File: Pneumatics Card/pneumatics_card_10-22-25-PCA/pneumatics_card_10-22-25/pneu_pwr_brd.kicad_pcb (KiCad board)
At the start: 2 copper layers, 47.6 x 53.5 mm, 38 parts, among them J1 2X1, J2 2X1, J3 2X1, J4 2X1, J5 2X1, J6 2X1, Q1 BSS138, Q2 BSS138, Q3 FQP30N06L, Q4 FQP30N06L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

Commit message: old pneumatics fixing PCB
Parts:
- removed J1: 2X1, Connector_JST:JST_PH_B2B-PH-K_1x02_P2.00mm_Vertical
- removed Q1, Q2: BSS138, Package_TO_SOT_SMD:SOT-23_Handsoldering
- removed R1, R2: 4.7k, Resistor_SMD:R_0805_2012Metric_Pad1.20x1.40mm_HandSolder
- removed REF** (x3): MountingHole_2.2mm_M2, MountingHole:MountingHole_2.2mm_M2
- added C10: 1uF, Capacitor_SMD:C_0402_1005Metric, F.Cu at (162.1, 31.2)
- added C11: 0.1uF, Capacitor_SMD:C_0402_1005Metric, F.Cu at (162.1, 33.2)
- added C12: 1uF, Capacitor_SMD:C_0402_1005Metric, F.Cu at (162.1, 35.2)
- added C13: 1uF, Capacitor_SMD:C_0402_1005Metric, F.Cu at (162.1, 37.1)
- added C14: 0.1uF, Capacitor_SMD:C_0402_1005Metric, F.Cu at (162.1, 39.1)
- added C16: 0.1u, Capacitor_SMD:C_0603_1608Metric, F.Cu at (153.5, 28.1)
- added C5: 1u, Capacitor_THT:CP_Radial_D5.0mm_P2.00mm, F.Cu at (173.8, 37.8)
- added C6: 0.1u, Capacitor_SMD:C_0603_1608Metric, F.Cu at (153.5, 25.6)
- added C7: 0.1uF, Capacitor_SMD:C_0402_1005Metric, F.Cu at (162.1, 25.3)
- added C8: 1uF, Capacitor_SMD:C_0402_1005Metric, F.Cu at (162.1, 27.3)
- added C9: 0.1uF, Capacitor_SMD:C_0402_1005Metric, F.Cu at (162.1, 29.2)
- added D5: 1N47xxA, Diode_THT:D_DO-41_SOD81_P10.16mm_Horizontal, F.Cu at (165.4, 26.4)
- added J7: 2X1, Connector_JST:JST_PH_B2B-PH-K_1x02_P2.00mm_Vertical, F.Cu at (166.5, 37.2)
- added Q7: IRF4905SPbF, Package_TO_SOT_THT:TO-220-3_Vertical, F.Cu at (166.8, 32.5)
- added R12: 100k, Resistor_SMD:R_0805_2012Metric_Pad1.20x1.40mm_HandSolder, F.Cu at (173.9, 42.5)
- added R13: 100k, Resistor_SMD:R_0805_2012Metric_Pad1.20x1.40mm_HandSolder, F.Cu at (173.9, 45.5)
- added R14: 10k, Resistor_SMD:R_0603_1608Metric, F.Cu at (153.5, 30.6)
- added R155: 10k, Resistor_SMD:R_0603_1608Metric, F.Cu at (153.5, 43.1)
- added R16: 10k, Resistor_SMD:R_0603_1608Metric, F.Cu at (153.5, 33.1)
- added R17: 10k, Resistor_SMD:R_0603_1608Metric, F.Cu at (153.5, 35.6)
- added R18: 10k, Resistor_SMD:R_0603_1608Metric, F.Cu at (153.5, 38.1)
- added R20: 10k, Resistor_SMD:R_0603_1608Metric, F.Cu at (153.5, 40.6)
- added U4: MCP1416, Package_TO_SOT_SMD:SOT-23-5, F.Cu at (158.1, 26.7)
- added U5: TCA4307, TCA4307:SOP65P490X110-8N, F.Cu at (167.8, 43.4)
- added U6: MCP1416, Package_TO_SOT_SMD:SOT-23-5, F.Cu at (158.1, 31.4)
- added U7: MCP1416, Package_TO_SOT_SMD:SOT-23-5, F.Cu at (158.1, 36.0)
- added U8: MCP1416, Package_TO_SOT_SMD:SOT-23-5, F.Cu at (158.1, 40.6)
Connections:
- F1 pad 2: SLN1+ -> Net-(D5-A)
- R10 pad 1: S4CTRL -> Net-(U8-OUT)
- R4 pad 1: S1CTRL -> Net-(U4-OUT)
- R6 pad 1: S2CTRL -> Net-(U6-OUT)
- R8 pad 1: S3CTRL -> Net-(U7-OUT)
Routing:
- net (no net): track 0.00 -> 48.5 mm
- net Net-(J1-Pin_2): track 29.8 -> 0.00 mm
- net Net-(J1-Pin_1): track 18.7 -> 0.00 mm

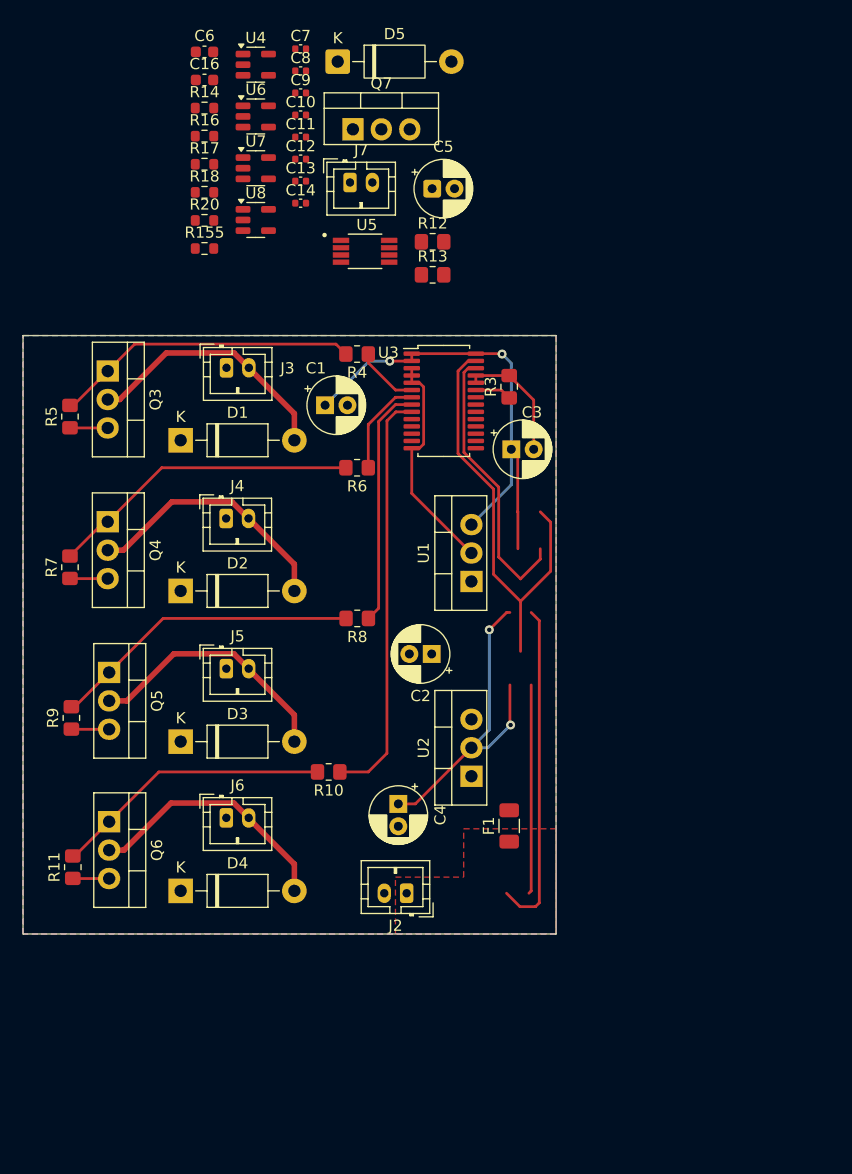
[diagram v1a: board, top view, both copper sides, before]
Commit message: added inrush protection to pcb
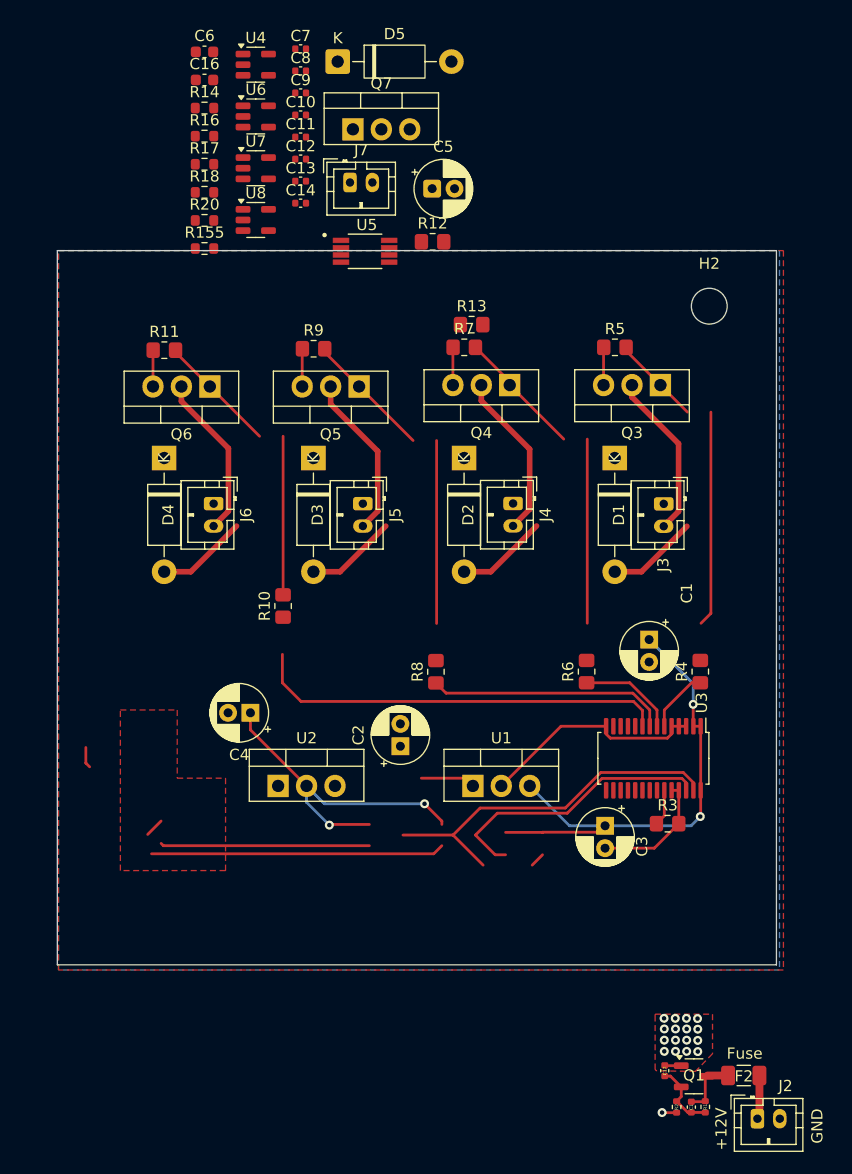
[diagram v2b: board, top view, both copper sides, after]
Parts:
- removed F1: 10A, Fuse:Fuse_1206_3216Metric
- added C1: 22nF, Capacitor_SMD:C_0402_1005Metric, F.Cu at (197.0, 119.9)
- added C12: 0.47u, Capacitor_SMD:C_0402_1005Metric, F.Cu at (194.6, 116.6)
- added F2: 10A, Fuse:Fuse_1206_3216Metric, F.Cu at (201.7, 117.0)
- added H2: MountingHole, MountingHole:MountingHole_3.2mm_M3_DIN965, F.Cu at (198.6, 48.3)
- added Q1: NTR0202PLT1G OR Si2347DS, Package_TO_SOT_SMD:SOT-23-3, F.Cu at (197.2, 117.1)
- added R1: 1k, Resistor_SMD:R_0402_1005Metric, F.Cu at (198.2, 119.8)
- added R2: 4.7k, Resistor_SMD:R_0402_1005Metric, F.Cu at (195.7, 119.8)
- moved Q3 49.4 mm to (194.2, 55.4), turned to 180 degrees
- moved R5 49.1 mm to (190.2, 52.0), turned to 0 degrees
- moved R11 46.9 mm to (149.9, 52.2), turned to 0 degrees
- moved R4 41.8 mm to (197.8, 81.0), turned to 90 degrees
- moved R3 41.5 mm to (194.9, 94.5), turned to 0 degrees
- moved J3 40.9 mm to (194.5, 66.0), turned to -90 degrees
- moved R7 40.3 mm to (176.7, 52.0), turned to 0 degrees
- moved Q6 39.9 mm to (154.0, 55.5), turned to 180 degrees
- moved R9 39.5 mm to (163.2, 52.1), turned to 0 degrees
- moved D1 38.8 mm to (190.2, 61.9), turned to -90 degrees
- moved D4 38.7 mm to (149.9, 61.9), turned to -90 degrees
- moved Q4 37.9 mm to (180.8, 55.4), turned to 180 degrees
- moved J2 37.3 mm to (202.9, 120.9), turned to 0 degrees
- moved U3 37.0 mm to (193.6, 88.7), turned to -90 degrees
- moved C1 35.7 mm to (193.2, 78.1), turned to -90 degrees
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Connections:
- J2 pad 1: Net-(J2-Pin_1) -> +12V_fuse
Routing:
- net (no net): track 48.5 -> 22.3 mm
- net SDA: track 38.8 -> 60.7 mm
- net Net-(Q1-G): track 0.00 -> 6.31 mm
- net Net-(Q1-S): track 0.00 -> 5.48 mm
- net SLN1+: track 1.06 -> 5.44 mm
- net +12V_fuse: track 0.00 -> 3.93 mm
- net 12V: track 0.00 -> 1.49 mm, vias 0 -> 16
- net GND: track 44.9 -> 46.2 mm, vias 0 -> 1
- added copper zone on F.Cu, net 12V
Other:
- board size 47.6 x 53.5 mm -> 64.2 x 63.8 mm
- board text added: "+12V"
- board text added: "Fuse"
- board text added: "GND"
